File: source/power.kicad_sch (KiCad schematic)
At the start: 101 parts, among them P5 PH_A, P6 GND, P7 SUPPLY, P8 PH_B, P9 PH_C, Q1 FMMT593TA, Q10 CSD19536KCS, Q11 CSD19536KCS, Q12 CSD19536KCS, Q13 FMMT593TA, Q14 FMMT593TA, Q15 CSD19536KCS, Q16 CSD19536KCS, Q17 CSD19536KCS, Q18 CSD19536KCS, Q2 FMMT593TA, Q3 NCEP60T20, Q4 CSD19536KCS, Q5 CSD19536KCS, Q6 CSD19536KCS, Q7 FMMT593TA, Q8 FMMT593TA, Q9 CSD19536KCS, U10 TP2604-SR, U9 TP2604-SR

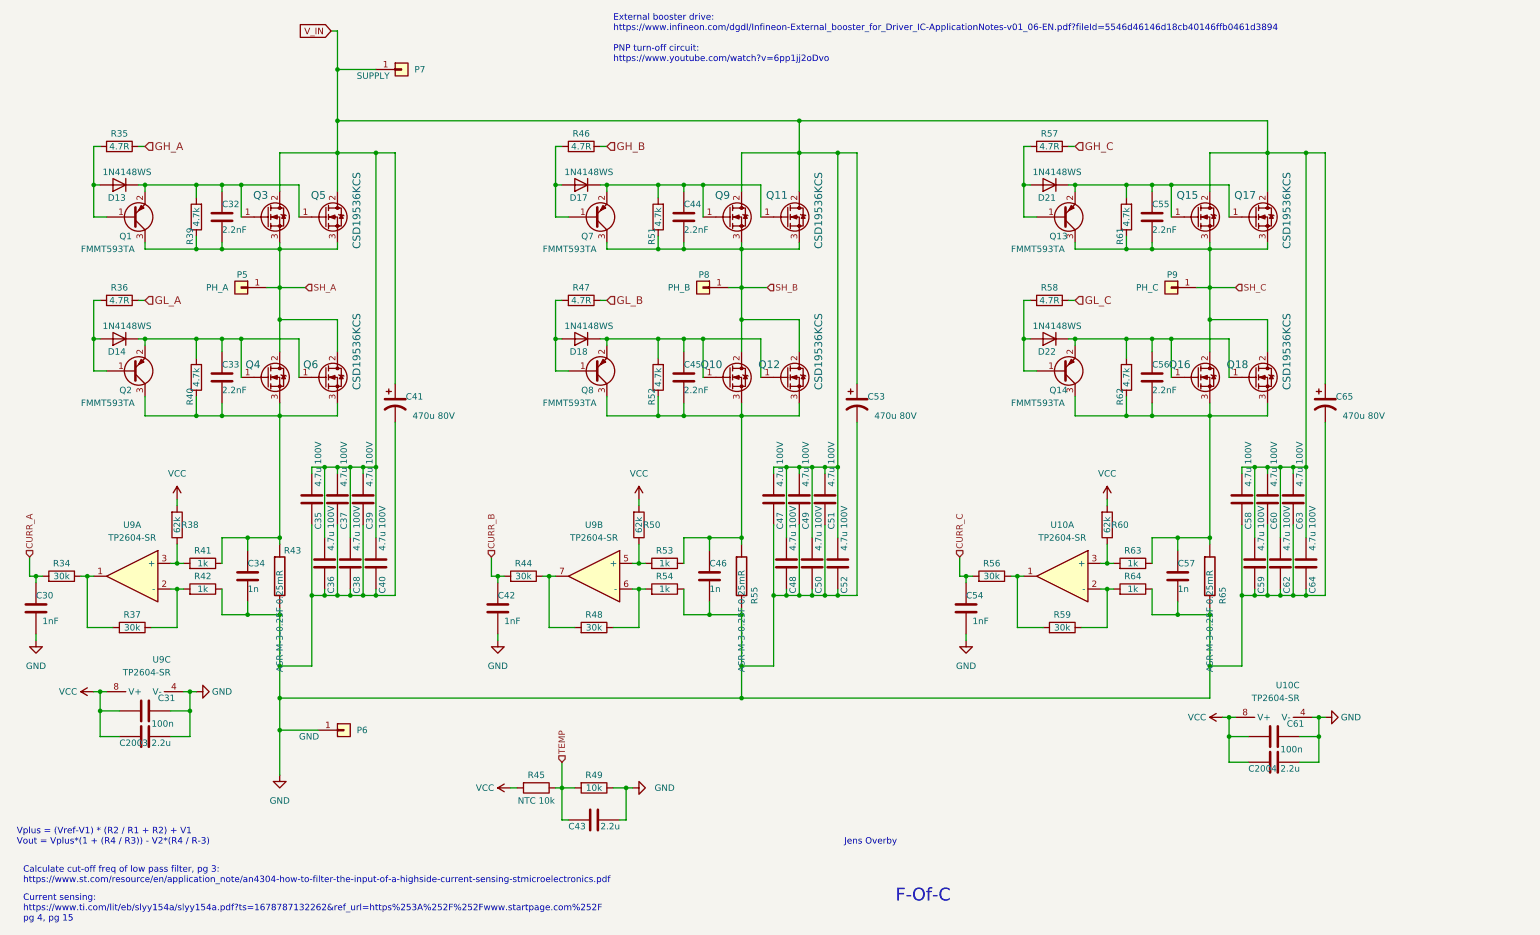
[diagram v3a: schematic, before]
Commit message: Most components now jlcpcb basic
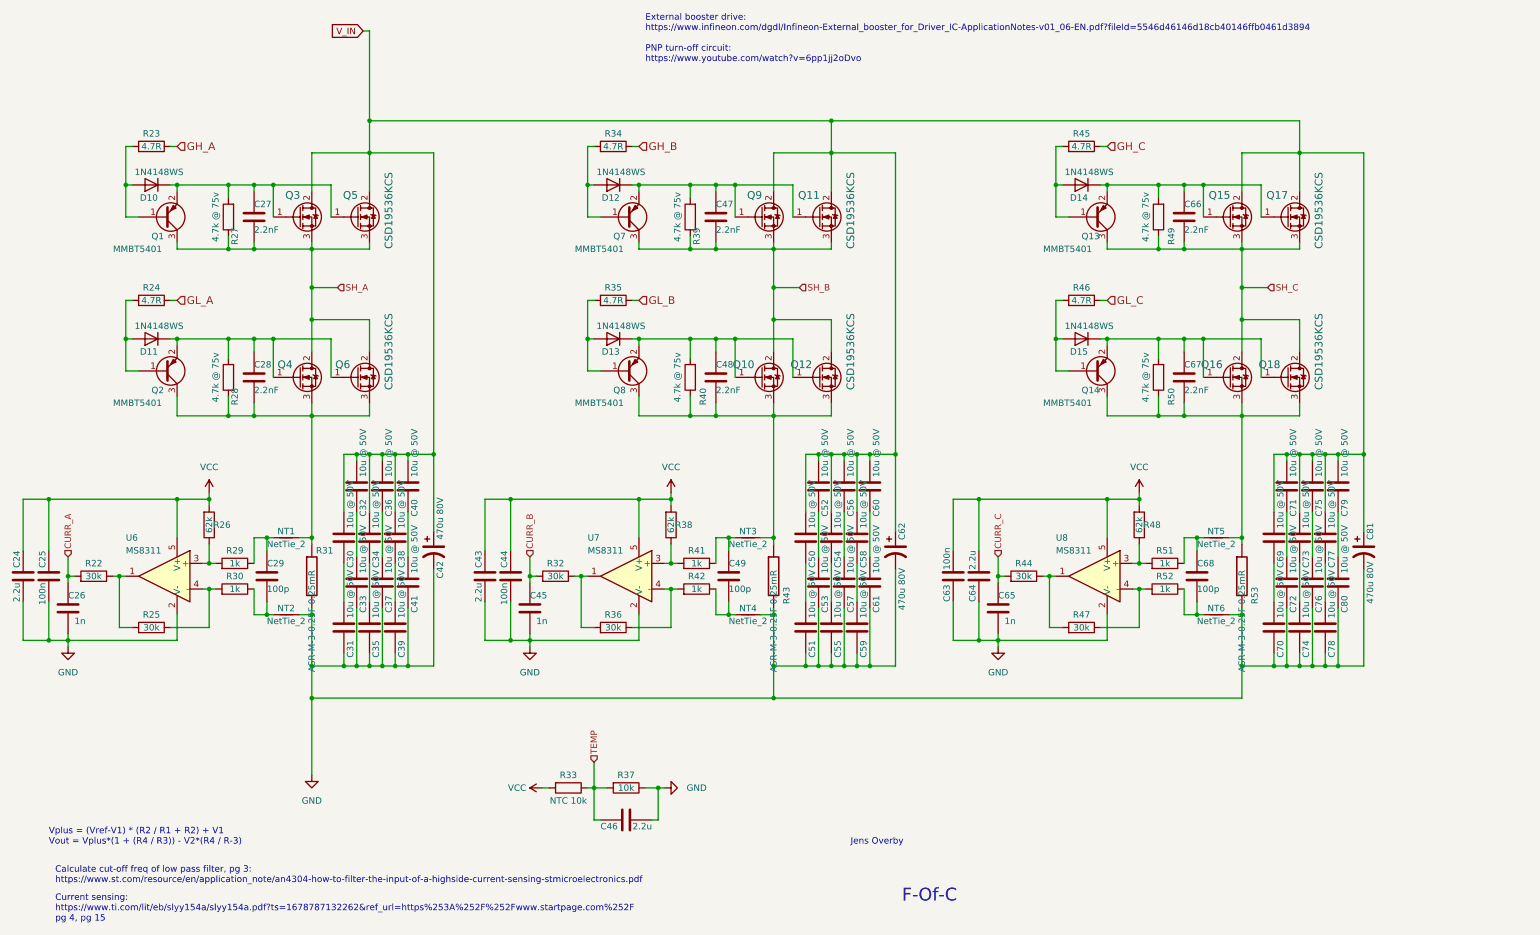
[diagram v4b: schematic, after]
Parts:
- removed C41, C65: 470u 80V, Capacitor_THT:CP_Radial_D8.0mm_P5.00mm, symbol Device:C_Polarized_US
- removed C48, C49, C50, C62, C63, C64: 4.7u 100V, Capacitor_SMD:C_0805_2012Metric, symbol BLDC_4-rescue:C-RESCUE-BLDC_4
- removed P5: PH_A, Connector:Banana_Jack_1Pin, symbol Connector_Generic:Conn_01x01
- removed P6: GND, Connector:Banana_Jack_1Pin, symbol Connector_Generic:Conn_01x01
- removed P7: SUPPLY, Connector:Banana_Jack_1Pin, symbol Connector_Generic:Conn_01x01
- removed P8: PH_B, Connector:Banana_Jack_1Pin, symbol Connector_Generic:Conn_01x01
- removed P9: PH_C, Connector:Banana_Jack_1Pin, symbol Connector_Generic:Conn_01x01
- removed U10, U9: TP2604-SR, Package_SO:SOIC-8_3.9x4.9mm_P1.27mm, symbol Custom_Library:TP2604-SR
- added C27: 2.2nF, Capacitor_SMD:C_0603_1608Metric, symbol BLDC_4-rescue:C-RESCUE-BLDC_4
- added C30, C31, C33, C34, C41, C53, C54, C55, C56, C57, C61, C69, C70, C71, C72, C73, C74, C75, C76, C77, C78, C79, C80: 10u @ 50V, Capacitor_SMD:C_1206_3216Metric, symbol BLDC_4-rescue:C-RESCUE-BLDC_4
- added C42, C81: 470u 80V, Custom:CP_Radial_D8.0mm_P5.00mm, symbol Device:C_Polarized_US
- added C43: 2.2u, Capacitor_SMD:C_0603_1608Metric, symbol BLDC_4-rescue:C-RESCUE-BLDC_4
- added C44: 100n, Capacitor_SMD:C_0402_1005Metric, symbol BLDC_4-rescue:C-RESCUE-BLDC_4
- added NT1, NT2, NT3, NT4, NT5, NT6: NetTie_2, NetTie:NetTie-2_SMD_Pad0.5mm, symbol Device:NetTie_2
- added U6: MS8311, Custom:SOT-23-5_MS8311, symbol Custom_Library:MS8311
- added U7, U8: MS8311, Package_TO_SOT_SMD:TSOT-23-5, symbol Amplifier_Operational:OPA188xxDBV
- C24: renamed from C2003; LCSC (none) -> C23630
- C25: renamed from C31; footprint Capacitor_SMD:C_0603_1608Metric -> Capacitor_SMD:C_0402_1005Metric; LCSC (none) -> C1525
- C26: renamed from C30; value 1nF -> 1n; footprint Capacitor_SMD:C_0603_1608Metric -> Capacitor_SMD:C_0402_1005Metric; LCSC (none) -> C1523
- C28: renamed from C33; LCSC (none) -> C77025
- C29: renamed from C34; value 1n -> 100p; LCSC (none) -> C14858
- C32: value 2.2nF -> 10u @ 50V; footprint Capacitor_SMD:C_0603_1608Metric -> Capacitor_SMD:C_1206_3216Metric; LCSC (none) -> C13585
- C35, C36, C37, C38, C39, C40, C51, C52, C58, C59, C60: value 4.7u 100V -> 10u @ 50V; footprint Capacitor_SMD:C_0805_2012Metric -> Capacitor_SMD:C_1206_3216Metric; LCSC (none) -> C13585
- C45: renamed from C42; value 1nF -> 1n; footprint Capacitor_SMD:C_0603_1608Metric -> Capacitor_SMD:C_0402_1005Metric; LCSC (none) -> C1523
- C46: renamed from C43; LCSC (none) -> C23630
- C47: renamed from C44; LCSC (none) -> C77025
- C48: renamed from C45; LCSC (none) -> C77025
- C49: renamed from C46; value 1n -> 100p; LCSC (none) -> C14858
- C50: renamed from C47; value 4.7u 100V -> 10u @ 50V; footprint Capacitor_SMD:C_0805_2012Metric -> Capacitor_SMD:C_1206_3216Metric; LCSC (none) -> C13585
- C62: renamed from C53; footprint Capacitor_THT:CP_Radial_D8.0mm_P5.00mm -> Custom:CP_Radial_D8.0mm_P5.00mm
- C63: renamed from C61; footprint Capacitor_SMD:C_0603_1608Metric -> Capacitor_SMD:C_0402_1005Metric; LCSC (none) -> C1525
- C64: renamed from C2004; LCSC (none) -> C23630
- C65: renamed from C54; value 1nF -> 1n; footprint Capacitor_SMD:C_0603_1608Metric -> Capacitor_SMD:C_0402_1005Metric; LCSC (none) -> C1523
- C66: renamed from C55; LCSC (none) -> C77025
- C67: renamed from C56; LCSC (none) -> C77025
- C68: renamed from C57; value 1n -> 100p; LCSC (none) -> C14858
- D10: renamed from D13; LCSC (none) -> C2128
- D11: renamed from D14; LCSC (none) -> C2128
- D12: renamed from D17; LCSC (none) -> C2128
- D13: renamed from D18; LCSC (none) -> C2128
- D14: renamed from D21; LCSC (none) -> C2128
- D15: renamed from D22; LCSC (none) -> C2128
- Q1, Q13, Q14, Q2, Q7, Q8: value FMMT593TA -> MMBT5401; LCSC (none) -> C8326
- R22: renamed from R34; footprint Resistor_SMD:R_0402_1005Metric -> Resistor_SMD:R_0603_1608Metric; LCSC (none) -> C22984
- R23: renamed from R35; footprint Resistor_SMD:R_0402_1005Metric -> Resistor_SMD:R_0603_1608Metric; LCSC (none) -> C23164
- R24: renamed from R36; footprint Resistor_SMD:R_0402_1005Metric -> Resistor_SMD:R_0603_1608Metric; LCSC (none) -> C23164
- R25: renamed from R37; footprint Resistor_SMD:R_0402_1005Metric -> Resistor_SMD:R_0603_1608Metric; LCSC (none) -> C22984
- R26: renamed from R38; footprint Resistor_SMD:R_0402_1005Metric -> Resistor_SMD:R_0603_1608Metric; LCSC (none) -> C23221
- R27: renamed from R39; value 4.7k -> 4.7k @ 75v; footprint Resistor_SMD:R_0402_1005Metric -> Resistor_SMD:R_0603_1608Metric; LCSC (none) -> C23162
- R28: renamed from R40; value 4.7k -> 4.7k @ 75v; footprint Resistor_SMD:R_0402_1005Metric -> Resistor_SMD:R_0603_1608Metric; LCSC (none) -> C23162
- R29: renamed from R41; LCSC (none) -> C11702
- R30: renamed from R42; LCSC (none) -> C11702
- R31: renamed from R43; LCSC (none) -> C495759
- R32: renamed from R44; footprint Resistor_SMD:R_0402_1005Metric -> Resistor_SMD:R_0603_1608Metric; LCSC (none) -> C22984
- R33: renamed from R45; footprint Resistor_SMD:R_0603_1608Metric -> Resistor_SMD:R_0402_1005Metric; LCSC (none) -> C13564
- R34: renamed from R46; footprint Resistor_SMD:R_0402_1005Metric -> Resistor_SMD:R_0603_1608Metric; LCSC (none) -> C23164
- R35: renamed from R47; footprint Resistor_SMD:R_0402_1005Metric -> Resistor_SMD:R_0603_1608Metric; LCSC (none) -> C23164
- R36: renamed from R48; footprint Resistor_SMD:R_0402_1005Metric -> Resistor_SMD:R_0603_1608Metric; LCSC (none) -> C22984
- R37: renamed from R49; LCSC (none) -> C25744
- R38: renamed from R50; footprint Resistor_SMD:R_0402_1005Metric -> Resistor_SMD:R_0603_1608Metric; LCSC (none) -> C23221
- R39: renamed from R51; value 4.7k -> 4.7k @ 75v; footprint Resistor_SMD:R_0402_1005Metric -> Resistor_SMD:R_0603_1608Metric; LCSC (none) -> C23162
- R40: renamed from R52; value 4.7k -> 4.7k @ 75v; footprint Resistor_SMD:R_0402_1005Metric -> Resistor_SMD:R_0603_1608Metric; LCSC (none) -> C23162
- R41: renamed from R53; LCSC (none) -> C11702
- R42: renamed from R54; LCSC (none) -> C11702
- R43: renamed from R55; LCSC (none) -> C495759
- R44: renamed from R56; footprint Resistor_SMD:R_0402_1005Metric -> Resistor_SMD:R_0603_1608Metric; LCSC (none) -> C22984
- R45: renamed from R57; footprint Resistor_SMD:R_0402_1005Metric -> Resistor_SMD:R_0603_1608Metric; LCSC (none) -> C23164
- R46: renamed from R58; footprint Resistor_SMD:R_0402_1005Metric -> Resistor_SMD:R_0603_1608Metric; LCSC (none) -> C23164
- R47: renamed from R59; footprint Resistor_SMD:R_0402_1005Metric -> Resistor_SMD:R_0603_1608Metric; LCSC (none) -> C22984
- R48: renamed from R60; footprint Resistor_SMD:R_0402_1005Metric -> Resistor_SMD:R_0603_1608Metric; LCSC (none) -> C23221
- R49: renamed from R61; value 4.7k -> 4.7k @ 75v; footprint Resistor_SMD:R_0402_1005Metric -> Resistor_SMD:R_0603_1608Metric; LCSC (none) -> C23162
- R50: renamed from R62; value 4.7k -> 4.7k @ 75v; footprint Resistor_SMD:R_0402_1005Metric -> Resistor_SMD:R_0603_1608Metric; LCSC (none) -> C23162
- R51: renamed from R63; LCSC (none) -> C11702
- R52: renamed from R64; LCSC (none) -> C11702
- R53: renamed from R65; LCSC (none) -> C495759
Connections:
- net GND: now also C63.2, C64.2, C31.1, C33.1, C41.1, C42.2, C43.1, C44.1, C53.1, C55.1, C57.1, C61.1, C70.1, C72.1, C74.1, C76.1, C78.1, C80.1, C81.2, NT2.2, NT4.2, NT6.2, U6.2 (V-), U7.2 (V-), U8.2 (V-); no longer C29.1, C36.1, C38.1, C40.1, C49.1, C50.1, C52.1, C58.1, C60.1, C63.1, C64.1, C68.1, R30.1, R42.1, R52.1
- net SH_A: now also C27.2; no longer C32.2
- net VCC: now also C63.1, C64.1, C43.2, C44.2, U6.5 (V+), U7.5 (V+), U8.5 (V+); no longer C63.2, C64.2
- net V_IN: now also C32.2, C30.2, C34.2, C42.1, C54.2, C56.2, C69.2, C71.2, C73.2, C75.2, C77.2, C79.2, C81.1; no longer C35.2, C37.2, C39.2, C51.2, C59.2
- net at C28.2, Q2.3 (C), Q4.3 (S)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: now also NT1.2; no longer C29.2, R29.1
- net at R26.1, R29.2: now also U6.3 (+)
- net at R25.1, R30.2: now also U6.4 (-)
- net at R22.1, R25.2: now also U6.1
- net at R44.1, R47.2: now also U8.1
- net at C67.2, Q14.3 (C), Q16.3 (S)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: now also NT5.2; no longer C68.2, R51.1
- net at C48.2, Q10.3 (S), Q12.3 (S)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: now also NT3.2; no longer C49.2, R41.1
- net at R38.1, R41.2: now also U7.3 (+)
- net at D10.1 (K), Q1.2 (E), Q3.1 (G)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: now also C27.1; no longer C32.1
- net at R47.1, R52.2: now also U8.4 (-)
- net at R36.1, R42.2: now also U7.4 (-)
- net at R32.1, R36.2: now also U7.1
- net at R48.1, R51.2: now also U8.3 (+)
- new net: C29.2, NT1.1, R29.1
- new net: C71.1, C72.2
- new net: C68.2, NT5.1, R51.1
- new net: C50.1, C51.2
- new net: C30.1, C31.2
- new net: C38.1, C39.2
- new net: C58.1, C59.2
- new net: C40.1, C41.2
- new net: C68.1, NT6.1, R52.1
- new net: C36.1, C37.2
- new net: C52.1, C53.2
- new net: C69.1, C70.2
- new net: C29.1, NT2.1, R30.1
- new net: C49.1, NT4.1, R42.1
- new net: C54.1, C55.2
- new net: C73.1, C74.2
- new net: C60.1, C61.2
- new net: C77.1, C78.2
- new net: C56.1, C57.2
- new net: C79.1, C80.2
- new net: C32.1, C33.2
- new net: C49.2, NT3.1, R41.1
- new net: C34.1, C35.2
- new net: C75.1, C76.2
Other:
- moved on the sheet: C24, C25, C26, C28, C29, C45, C46, C47, C48, C49, C50, C62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

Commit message: Add files via upload
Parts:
- C25, C44, C63: footprint Capacitor_SMD:C_0402_1005Metric -> Capacitor_SMD:C_0603_1608Metric; LCSC C1525 -> C14663
- C26, C45, C65: footprint Capacitor_SMD:C_0402_1005Metric -> Capacitor_SMD:C_0603_1608Metric; LCSC C1523 -> C1588
- R28: renamed from R29; footprint Resistor_SMD:R_0402_1005Metric -> Resistor_SMD:R_0603_1608Metric; LCSC C11702 -> C21190
- R29: renamed from R30; footprint Resistor_SMD:R_0402_1005Metric -> Resistor_SMD:R_0603_1608Metric; LCSC C11702 -> C21190
- R40: renamed from R41; footprint Resistor_SMD:R_0402_1005Metric -> Resistor_SMD:R_0603_1608Metric; LCSC C11702 -> C21190
- R41: renamed from R42; footprint Resistor_SMD:R_0402_1005Metric -> Resistor_SMD:R_0603_1608Metric; LCSC C11702 -> C21190
- R50: renamed from R51; footprint Resistor_SMD:R_0402_1005Metric -> Resistor_SMD:R_0603_1608Metric; LCSC C11702 -> C21190
- R51: renamed from R52; footprint Resistor_SMD:R_0402_1005Metric -> Resistor_SMD:R_0603_1608Metric; LCSC C11702 -> C21190
- renumbered R22 to R21, R23 to R22, R24 to R23, R25 to R24, R26 to R25, R27 to R26, R28 to R27, R31 to R30, R32 to R31, R33 to R32, R34 to R33, R35 to R34, R36 to R35, R37 to R36, R38 to R37, R39 to R38, R40 to R39, R43 to R42, R44 to R43, R45 to R44, R46 to R45, R47 to R46, R48 to R47, R49 to R48, R50 to R49, R53 to R52
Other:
- moved on the sheet: C63, C64
